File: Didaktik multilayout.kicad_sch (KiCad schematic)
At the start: 123 parts, among them J1 Conn_01x04_MountingPin, J2 AVR-ISP-6, J3 Conn_01x03, SW1 SW_Push_45deg, SW10 SW_Push_45deg, SW11 SW_Push_45deg, SW12 SW_Push_45deg, SW13 SW_Push_45deg, SW14 SW_Push_45deg, SW15 SW_Push_45deg, SW16 SW_Push_45deg, SW17 SW_Push_45deg, SW18 SW_Push_45deg, SW19 SW_Push_45deg, SW2 SW_Push_45deg, SW20 SW_Push_45deg, SW21 SW_Push_45deg, SW22 SW_Push_45deg, SW23 SW_Push_45deg, SW24 SW_Push_45deg, SW25 SW_Push_45deg, SW26 SW_Push_45deg, SW27 SW_Push_45deg, SW28 SW_Push_45deg, SW29 SW_Push_45deg, SW3 SW_Push_45deg, SW30 SW_Push_45deg, SW31 SW_Push_45deg, SW31a1 SW_Push_45deg, SW32 SW_Push_45deg, SW32a1 SW_Push_45deg, SW33 SW_Push_45deg, SW33a1 SW_Push_45deg, SW34 SW_Push_45deg, SW34a1 SW_Push_45deg, SW34b1 SW_Push_45deg, SW35 SW_Push_45deg, SW35a1 SW_Push_45deg, SW35b1 SW_Push_45deg, SW35c1 SW_Push_45deg, SW36 SW_Push_45deg, SW36a1 SW_Push_45deg, SW36b1 SW_Push_45deg, SW36c1 SW_Push_45deg, SW37 SW_Push_45deg, SW37a1 SW_Push_45deg, SW37b1 SW_Push_45deg, SW38 SW_Push_45deg, SW38a1 SW_Push_45deg, SW39 SW_Push_45deg, SW39a1 SW_Push_45deg, SW4 SW_Push_45deg, SW40 SW_Push_45deg, SW40a1 SW_Push_45deg, SW41 RotaryEncoder_Switch, SW42 RotaryEncoder_Switch, SW5 SW_Push_45deg, SW6 SW_Push_45deg, SW7 SW_Push_45deg, SW8 SW_Push_45deg, SW9 SW_Push_45deg, U1 ATmega32U4-M, Y1 Crystal_GND24_Small

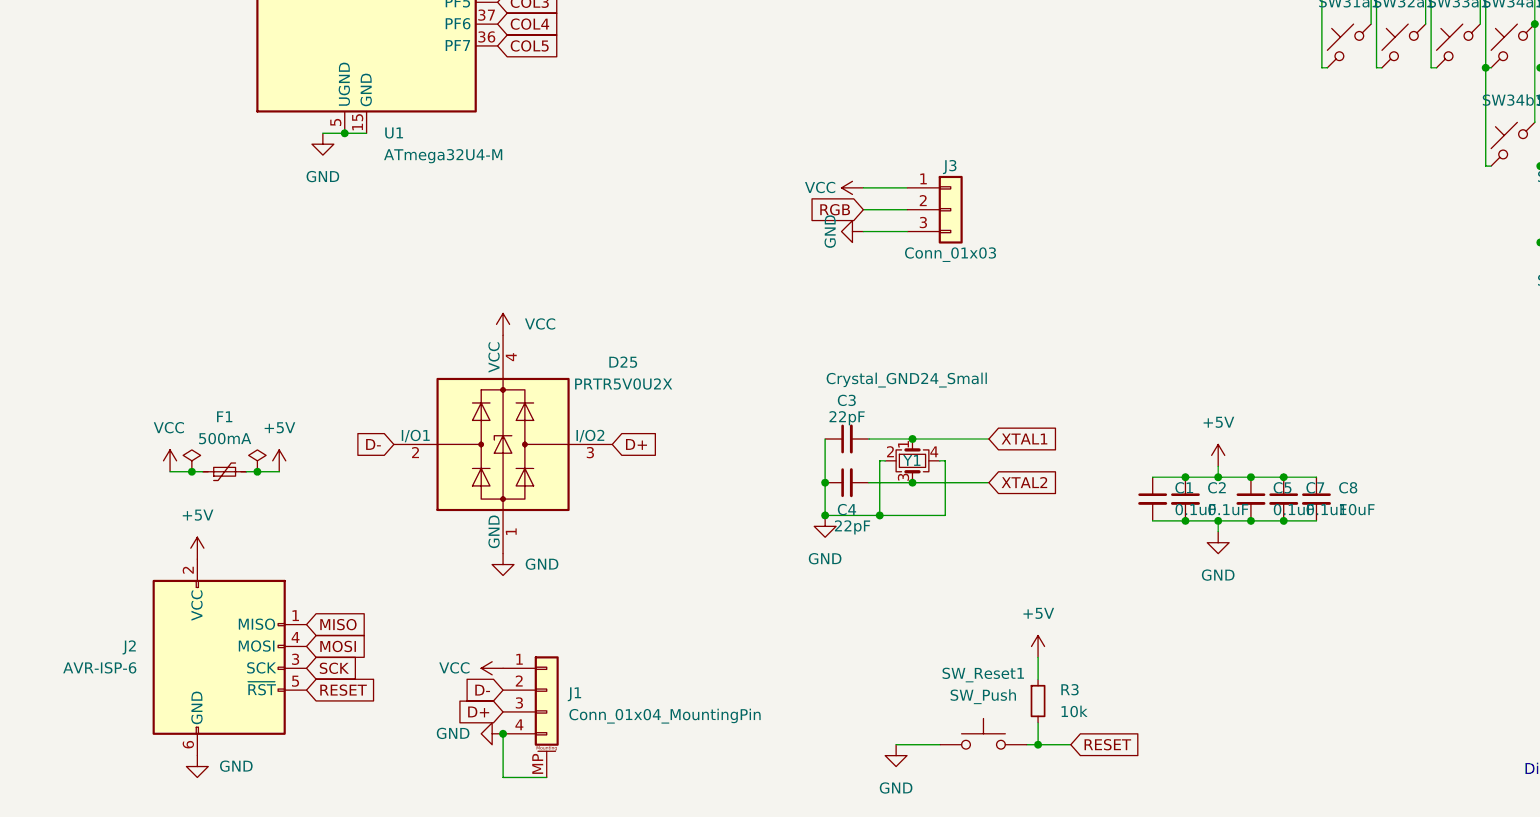
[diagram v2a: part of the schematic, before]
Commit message: cleaned up routing
sudden 9th error isp ground via to gnd net?
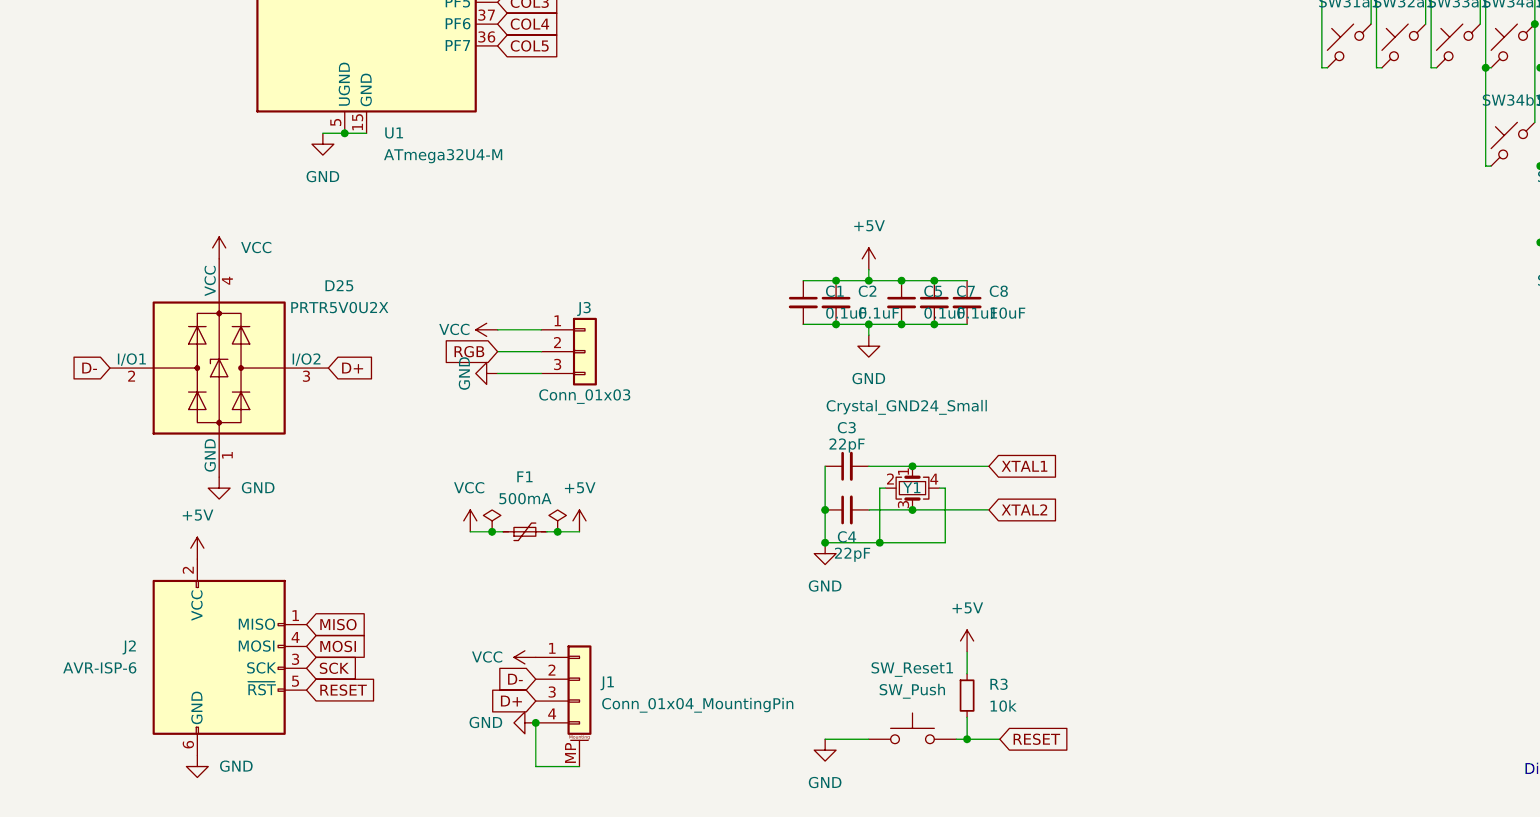
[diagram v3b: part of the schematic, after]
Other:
- moved on the sheet: C1, C2, C3, C4, C5, C7, C8, D25, F1, J1, J3, R3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

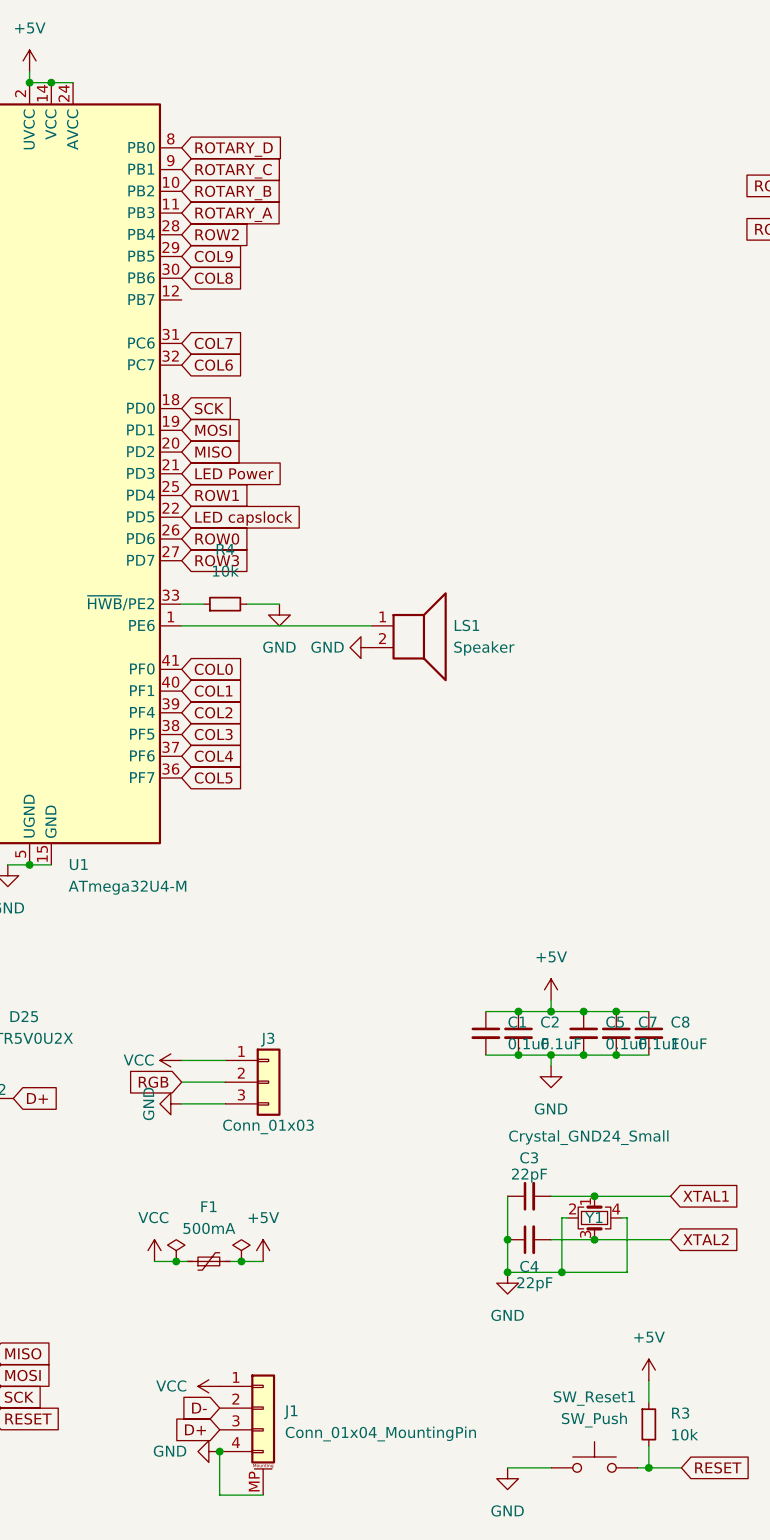
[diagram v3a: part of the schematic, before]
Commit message: edited buzzer schematics & pcb placement
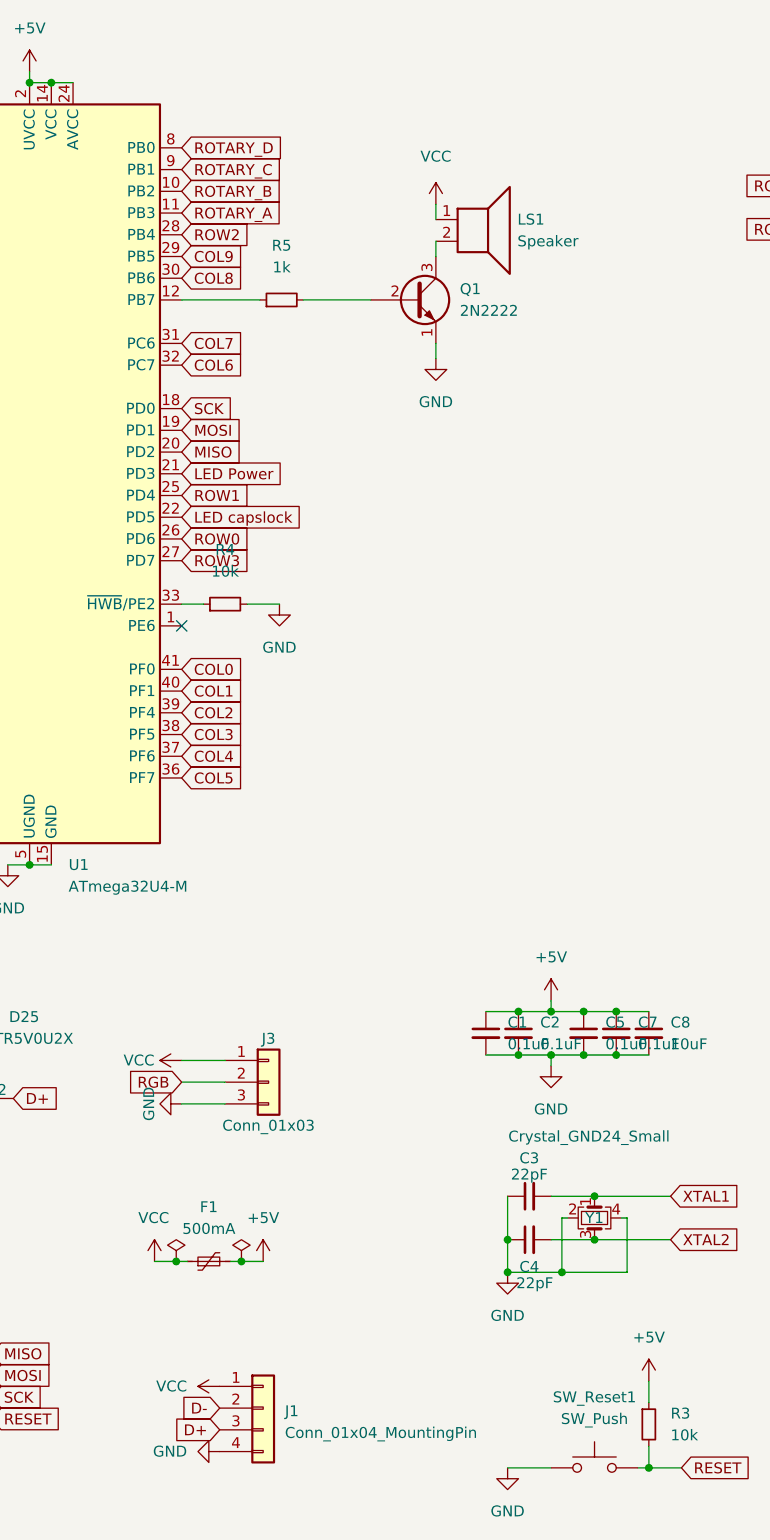
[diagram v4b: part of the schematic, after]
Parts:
- added Q1: 2N2222, Package_TO_SOT_SMD:SOT-23, symbol Transistor_BJT:2N2219
- added R5: 1k, Keebio-Parts:Diode-Hybrid-Back, symbol Device:R_Small
- J1: symbol Connector_Generic_MountingPin:Conn_01x04_MountingPin -> Connector_Generic:Conn_01x04
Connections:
- net GND: now also Q1.1 (E); no longer J1.MP (MountPin), LS1.2
- net VCC: now also LS1.1
- net at U1.1 (PE6): no longer LS1.1
- net at U1.12 (PB7): now also R5.1
- new net: LS1.2, Q1.3 (C)
- new net: Q1.2 (B), R5.2
- no-connect marks 0 -> 1

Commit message: new production files
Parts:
- added R6: 1k, Resistor_SMD:R_0402_1005Metric, symbol Device:R_Small
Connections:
- net VCC: now also R6.1
- net at LS1.2, Q1.3 (C): now also R6.2
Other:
- moved on the sheet: LS1
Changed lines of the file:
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@@
   (junction (at 171.45 88.265) (diameter 0) (color 0 0 0 0)
   )
+  (junction (at 98.298 35.56) (diameter 0) (color 0 0 0 0)
+  )
   (junction (at 214.63 57.15) (diameter 0) (color 0 0 0 0)
   )
@@
   (junction (at 208.28 102.87) (diameter 0) (color 0 0 0 0)
   )
+  (junction (at 98.298 40.64) (diameter 0) (color 0 0 0 0)
+  )
   (junction (at 196.85 93.345) (diameter 0) (color 0 0 0 0)
   )
@@
     (stroke (width 0) (type default) (color 0 0 0 0))
   )
+  (wire (pts (xy 98.298 31.75) (xy 98.298 35.56))
+    (stroke (width 0) (type default) (color 0 0 0 0))
+  )
   (wire (pts (xy 68.58 85.09) (xy 71.12 85.09))
     (stroke (width 0) (type default) (color 0 0 0 0))
@@
     (stroke (width 0) (type default) (color 0 0 0 0))
   )
+  (wire (pts (xy 103.886 36.83) (xy 103.886 35.56))
+    (stroke (width 0) (type default) (color 0 0 0 0))
+  )
   (wire (pts (xy 220.98 83.185) (xy 220.98 102.87))
     (stroke (width 0) (type default) (color 0 0 0 0))
@@
     (stroke (width 0) (type default) (color 0 0 0 0))
   )
+  (wire (pts (xy 103.886 35.56) (xy 98.298 35.56))
+    (stroke (width 0) (type default) (color 0 0 0 0))
+  )
   (wire (pts (xy 170.18 69.85) (xy 170.18 57.15))
     (stroke (width 0) (type default) (color 0 0 0 0))
@@
     (stroke (width 0) (type default) (color 0 0 0 0))
   )
+  (wire (pts (xy 98.298 40.64) (xy 103.886 40.64))
+    (stroke (width 0) (type default) (color 0 0 0 0))
+  )
   (wire (pts (xy 209.55 80.01) (xy 203.2 80.01))
     (stroke (width 0) (type default) (color 0 0 0 0))
@@
     (stroke (width 0) (type default) (color 0 0 0 0))
   )
+  (wire (pts (xy 98.298 40.64) (xy 98.298 44.45))
+    (stroke (width 0) (type default) (color 0 0 0 0))
+  )
   (wire (pts (xy 215.9 93.345) (xy 222.25 93.345))
     (stroke (width 0) (type default) (color 0 0 0 0))
@@
     (stroke (width 0) (type default) (color 0 0 0 0))
   )
-  (wire (pts (xy 98.298 38.354) (xy 98.298 40.132))
-    (stroke (width 0) (type default) (color 0 0 0 0))
-  )
   (wire (pts (xy 189.23 69.85) (xy 189.23 83.185))
     (stroke (width 0) (type default) (color 0 0 0 0))
@@
     (stroke (width 0) (type default) (color 0 0 0 0))
   )
+  (wire (pts (xy 103.886 40.64) (xy 103.886 39.37))
+    (stroke (width 0) (type default) (color 0 0 0 0))
+  )
   (wire (pts (xy 208.915 107.95) (xy 209.55 107.95))
     (stroke (width 0) (type default) (color 0 0 0 0))
@@
     (stroke (width 0) (type default) (color 0 0 0 0))
   )
-  (wire (pts (xy 98.298 42.672) (xy 98.298 44.45))
-    (stroke (width 0) (type default) (color 0 0 0 0))
-  )
   (wire (pts (xy 184.15 67.31) (xy 177.8 67.31))
     (stroke (width 0) (type default) (color 0 0 0 0))
@@
     (pin "2")
   )
-  (symbol (lib_id "Device:Speaker") (at 103.378 40.132 0) (unit 1)
+  (symbol (lib_id "Device:Speaker") (at 108.966 36.83 0) (unit 1)
     (in_bom yes) (on_board yes) (fields_autoplaced)
-    (property "Reference" "LS1" (id 0) (at 107.823 40.1319 0)
+    (property "Reference" "LS1" (id 0) (at 113.411 36.8299 0)
       (effects (font (size 1.27 1.27)) (justify left))
     )
-    (property "Value" "Speaker" (id 1) (at 107.823 42.6719 0)
+    (property "Value" "Speaker" (id 1) (at 113.411 39.3699 0)
       (effects (font (size 1.27 1.27)) (justify left))
     )
-    (property "Footprint" "Keebio-Parts:AST1109MLTRQ" (id 2) (at 103.378 45.212 0)
+    (property "Footprint" "Keebio-Parts:AST1109MLTRQ" (id 2) (at 108.966 41.91 0)
       (effects (font (size 1.27 1.27)) hide)
     )
-    (property "Datasheet" "~" (id 3) (at 103.124 41.402 0)
+    (property "Datasheet" "~" (id 3) (at 108.712 38.1 0)
       (effects (font (size 1.27 1.27)) hide)
     )
@@
     (pin "1")
   )
-  (symbol (lib_id "power:VCC") (at 98.298 38.354 0) (unit 1)
+  (symbol (lib_id "power:VCC") (at 98.298 31.75 0) (unit 1)
     (in_bom yes) (on_board yes) (fields_autoplaced)
-    (property "Reference" "#PWR0126" (id 0) (at 98.298 42.164 0)
+    (property "Reference" "#PWR0126" (id 0) (at 98.298 35.56 0)
       (effects (font (size 1.27 1.27)) hide)
     )
-    (property "Value" "VCC" (id 1) (at 98.298 32.766 0))
-    (property "Footprint" "" (id 2) (at 98.298 38.354 0)
+    (property "Value" "VCC" (id 1) (at 98.298 26.162 0))
+    (property "Footprint" "" (id 2) (at 98.298 31.75 0)
       (effects (font (size 1.27 1.27)) hide)
     )
-    (property "Datasheet" "" (id 3) (at 98.298 38.354 0)
+    (property "Datasheet" "" (id 3) (at 98.298 31.75 0)
       (effects (font (size 1.27 1.27)) hide)
     )
@@
     (pin "2")
   )
+  (symbol (lib_id "Device:R_Small") (at 98.298 38.1 0) (unit 1)
+    (in_bom yes) (on_board yes) (fields_autoplaced)
+    (property "Reference" "R6" (id 0) (at 100.076 36.8299 0)
+      (effects (font (size 1.27 1.27)) (justify left))
+    )
+    (property "Value" "1k" (id 1) (at 100.076 39.3699 0)
+      (effects (font (size 1.27 1.27)) (justify left))
+    )
+    (property "Footprint" "Resistor_SMD:R_0402_1005Metric" (id 2) (at 98.298 38.1 0)
+      (effects (font (size 1.27 1.27)) hide)
+    )
+    (property "Datasheet" "~" (id 3) (at 98.298 38.1 0)
+      (effects (font (size 1.27 1.27)) hide)
+    )
+    (pin "1")
+    (pin "2")
+  )
   (symbol (lib_id "Switch:SW_Push_45deg") (at 205.74 116.84 0) (mirror y) (unit 1)
     (in_bom yes) (on_board yes)
@@
       (reference "R5") (unit 1) (value "1k") (footprint "Keebio-Parts:Diode-Hybrid-Back")
     )
+    (path "/99bcff19-9eea-4c2e-9a3a-3f6d83568116"
+      (reference "R6") (unit 1) (value "1k") (footprint "Resistor_SMD:R_0402_1005Metric")
+    )
     (path "/aa3e1884-38d9-45ba-ac50-ac00233610fb"
